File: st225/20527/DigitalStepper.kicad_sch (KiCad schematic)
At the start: 63 parts, among them J3 POWER, J6 STEPPER, Q9 2N3906, Y1 2MHz

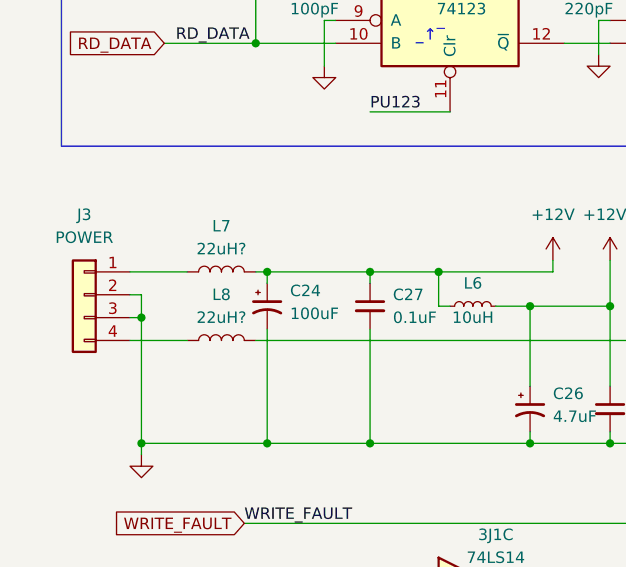
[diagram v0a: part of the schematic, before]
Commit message: Add some part values to 20527
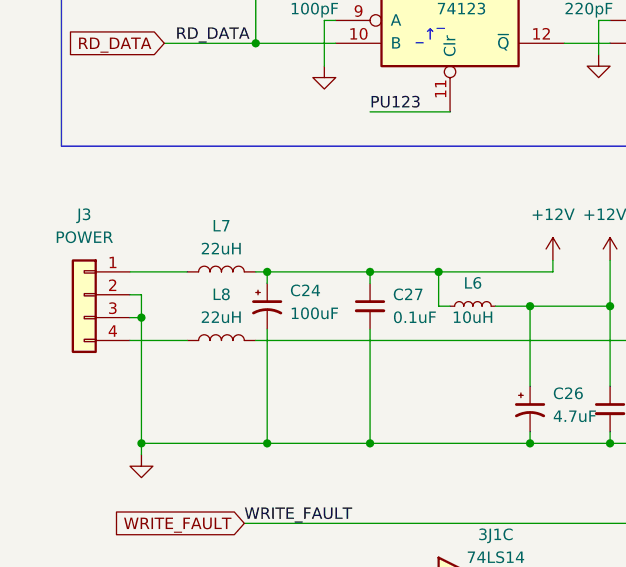
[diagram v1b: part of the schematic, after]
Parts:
- L7, L8: value 22uH? -> 22uH
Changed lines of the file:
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@@
       (effects (font (size 1.27 1.27) (color 255 0 255 1)))
     )
-    (property "Value" "22uH?" (at 30.48 194.31 90)
+    (property "Value" "22uH" (at 30.48 194.31 90)
       (effects (font (size 1.27 1.27)))
     )
@@
       (effects (font (size 1.27 1.27) (color 255 0 255 1)))
     )
-    (property "Value" "22uH?" (at 30.48 201.93 90)
-      (effects (font (size 1.27 1.27)))
-    )
+    (property "Value" "22uH" (at 30.48 201.93 90)
+      (effects (font (size 1.27 1.27)))
+    )

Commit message: st225 updates with more info
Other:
- note added: "RD_DATA DC: PA7 = low RD_DATA f < 1.4MHz: PA7 = pulsing RD_DATA 1.4MHz < f < 2.6MHz: PA7 = high RD_DATA f > 2.6MHz: PA7 = low"
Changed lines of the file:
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@@
+    (effects (font (size 1.27 1.27)) (justify left bottom))
+  )
+  (text "RD_DATA DC: PA7 = low\nRD_DATA f < 1.4MHz: PA7 = pulsing\nRD_DATA 1.4MHz < f < 2.6MHz: PA7 = high\nRD_DATA f > 2.6MHz: PA7 = low"
+    (at 50.8 146.05 0)
     (effects (font (size 1.27 1.27)) (justify left bottom))
   )
